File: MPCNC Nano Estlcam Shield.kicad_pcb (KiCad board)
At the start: 2 copper layers, 160 x 100 mm, 92 parts, among them J1 Screw_Terminal_01x02, J10 Conn_01x04_Male, J11 Conn_01x04_Male, J12 Screw_Terminal_01x03, J13 Screw_Terminal_01x03, J14 Screw_Terminal_01x03, J15 Conn_02x03_Odd_Even, J16 Screw_Terminal_01x02, J17 Screw_Terminal_01x02, J18 Screw_Terminal_01x03, J19 Screw_Terminal_01x03, J2 Conn_01x03_Male, J20 Screw_Terminal_01x03, J21 Screw_Terminal_01x03, J22 Screw_Terminal_01x03, J23 Screw_Terminal_01x03, J24 Screw_Terminal_01x03, J25 Screw_Terminal_01x03, J26 Screw_Terminal_01x03, J27 Screw_Terminal_01x03, J28 Conn_01x03_Male, J29 Conn_01x02_Male, J3 Conn_01x06_Male, J4 Screw_Terminal_01x03, J5 Screw_Terminal_01x03, J6 Screw_Terminal_01x03, J7 Conn_01x04_Male, J8 Conn_01x04_Male, J9 Conn_01x04_Male, U1 LM358, U2 LTV-847, U3 LTV-847, U4 LTV-847, U5 ULN2003, U6 L7805, U7 ATtiny45-20PU

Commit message: V1.3
- Version 1.3 of MPCNC Nano Estlcam Shield
   PCB schematic changes:
    # Changed electrolytic capacitor values for L7805 (0,33µF + 0,1µF)
   PCB layout changes:
    # Changed footprint of electrolytic capacitor for L7805 (D=8mm/RM=3,5mm -> D=5mm/RM=2,0mm)
    # Revised heatsink footprint
    + Footprints for many components added to project footprint library ("MPCNC_Shield_Footprints"). Modified footprints from standard KiCad library with value on
silkscreen
    + Added "Uncle Phil" logo on backside silk screen layer
    + Added jumper function description on frontside silk screen layer
    # Changed mounting holes (Edge.cut layer -> footprint)
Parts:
- added H1: MountingHole, MountingHole:MountingHole_4.3mm_M4_DIN965_Pad, F.Cu at (65.5, 137.3)
- added H2: MountingHole, MountingHole:MountingHole_4.3mm_M4_DIN965_Pad, F.Cu at (217.5, 137.3)
- added H3: MountingHole, MountingHole:MountingHole_4.3mm_M4_DIN965_Pad, F.Cu at (217.5, 45.4)
- added H4: MountingHole, MountingHole:MountingHole_4.3mm_M4_DIN965_Pad, F.Cu at (65.5, 45.4)
- A1: value Arduino_Nano_v3.x -> Arduino Nano
- C1, C2, C3, C4: footprint Capacitor_THT:CP_Radial_D8.0mm_P3.50mm -> MPCNC_Shield_Footprints:CP_Radial_D8.0mm_P3.50mm
- C5: value 1µF -> 0,33µF; footprint Capacitor_THT:CP_Radial_D8.0mm_P3.50mm -> Capacitor_THT:CP_Radial_D5.0mm_P2.00mm
- C6: value 1µF -> 0,1µF; footprint Capacitor_THT:CP_Radial_D8.0mm_P3.50mm -> Capacitor_THT:CP_Radial_D5.0mm_P2.00mm
- D2, D3: footprint Diode_THT:D_DO-201AD_P15.24mm_Horizontal -> MPCNC_Shield_Footprints:D_DO-201AD_P15.24mm_Horizontal
- R1, R10, R11, R12, R13, R14, R15, R16, R17, R18, R2, R3, R4, R5, R6, R7, R8, R9: footprint Resistor_THT:R_Axial_DIN0207_L6.3mm_D2.5mm_P7.62mm_Horizontal -> MPCNC_Shield_Footprints:R_Axial_DIN0207_L6.3mm_D2.5mm_P7.62mm_Horizontal
- U1: footprint Package_DIP:DIP-8_W7.62mm -> MPCNC_Shield_Footprints:DIP-8_W7.62mm
- U2, U3, U4, U5: footprint Package_DIP:DIP-16_W7.62mm -> MPCNC_Shield_Footprints:DIP-16_W7.62mm
- U7: footprint Package_DIP:DIP-8_W7.62mm_LongPads -> MPCNC_Shield_Footprints:DIP-8_W7.62mm
- moved R14 6.35 mm to (180.9, 103.9), turned to 0 degrees
- moved C5 3.70 mm to (163.1, 93.7)
- moved JP13 0.25 mm to (207.6, 129.9)
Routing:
- net /D1_R_LED: track 24.7 -> 15.8 mm
- net +5V: track 685.5 -> 679.4 mm
- net +12V: track 135.3 -> 132.0 mm
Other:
- outline, holes or cut-outs redrawn
- board text added: "12V"
- board text added: "5V"
- board text added: "5V/10V"
- board text added: "Adjust 0-10V"
- board text added: "Analog"
- board text added: "COM"
- board text added: "FLT"
- board text added: "Fan 12V"
- board text added: "ICSP"
- board text added: "MPCNC Nano Estlcam Shield © V1.3"
- board text added: "PWM"
- board text added: "Spindle On/Off"
- board text removed: "Adjust to 0-10V"
- board text removed: "FAN 12V"
- board text removed: "MPCNC Nano Estlcam Shield © V1.2"

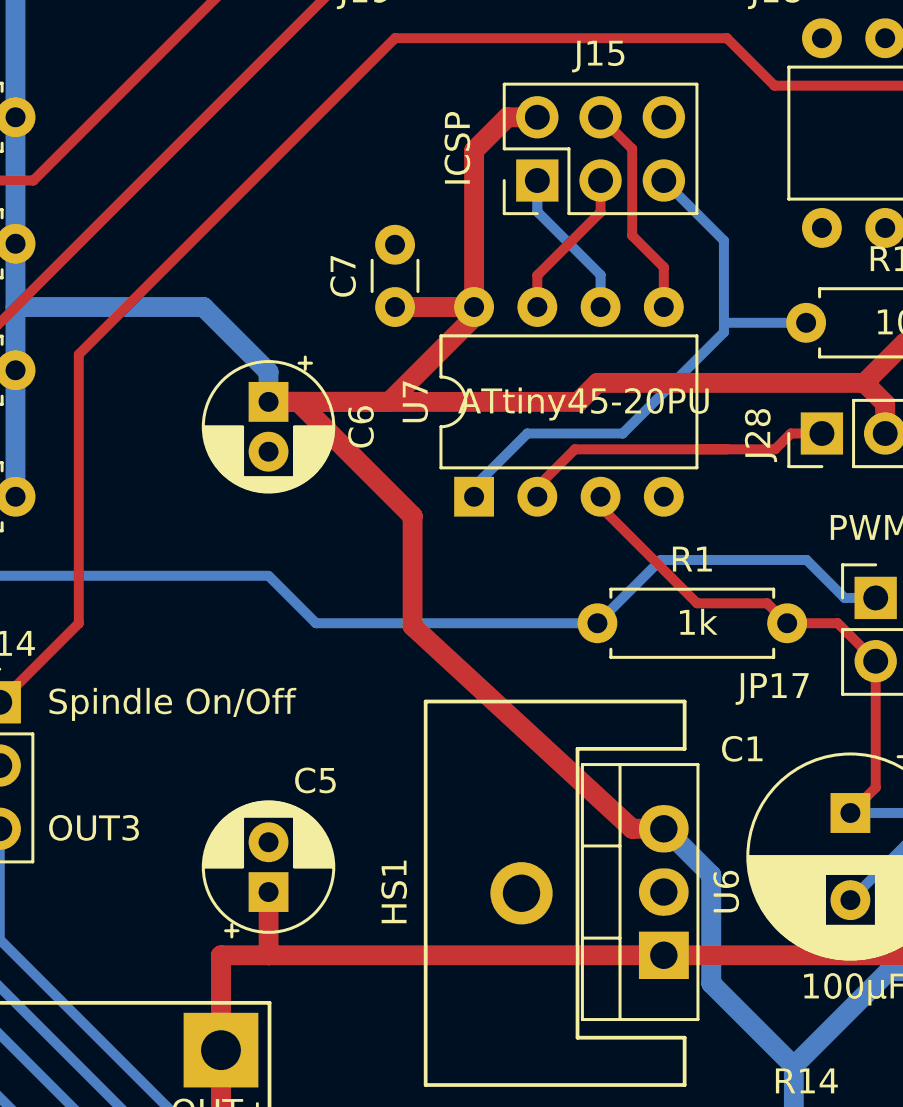
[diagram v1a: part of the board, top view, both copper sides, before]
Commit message: Minor changes for V1.3
   PCB schematic changes:
#Changed footprints for some parts from standard lib to MPCNC lib
   PCB layout changes:
#Added value to silk screen layer for some footprints
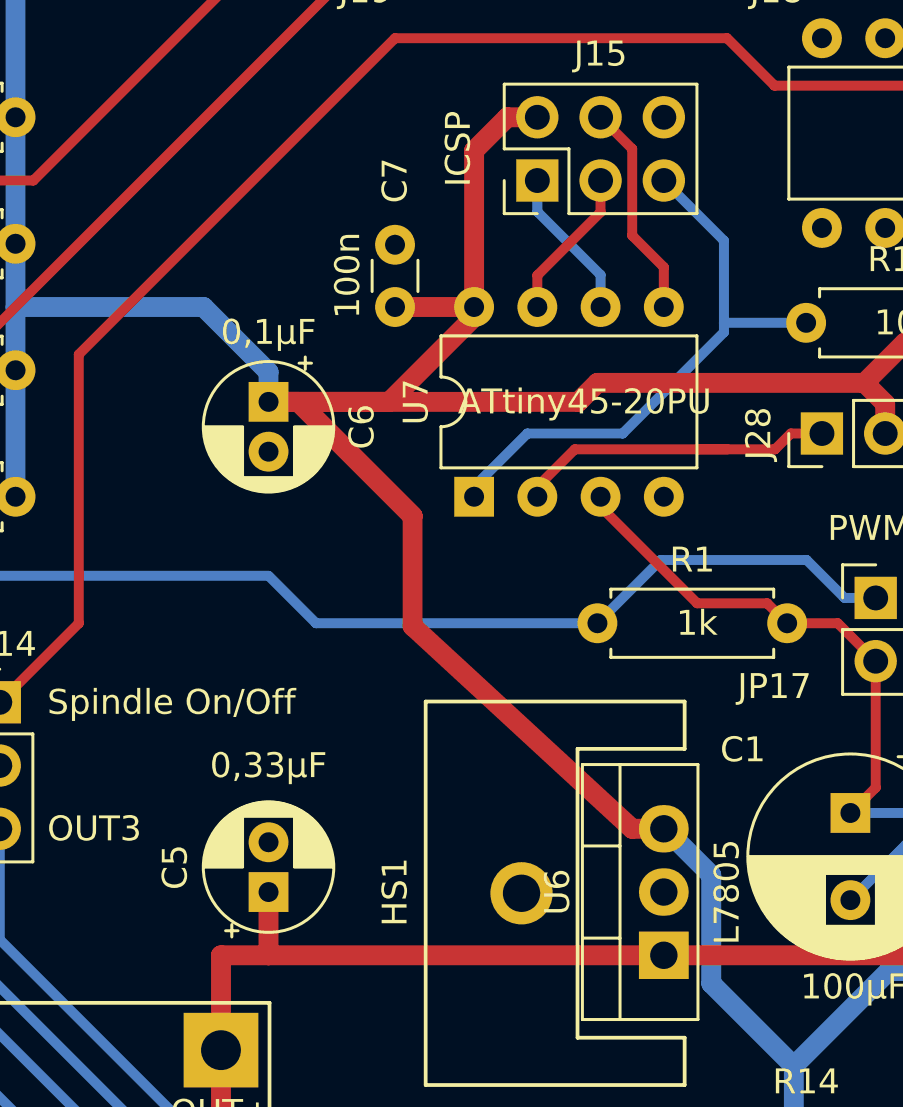
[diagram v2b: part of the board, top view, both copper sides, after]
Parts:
- C5, C6: footprint Capacitor_THT:CP_Radial_D5.0mm_P2.00mm -> MPCNC_Shield_Footprints:CP_Radial_D5.0mm_P2.00mm
- C7: footprint Capacitor_THT:C_Disc_D3.0mm_W1.6mm_P2.50mm -> MPCNC_Shield_Footprints:C_Disc_D3.0mm_W1.6mm_P2.50mm
- U6: footprint Package_TO_SOT_THT:TO-220-3_Vertical -> MPCNC_Shield_Footprints:TO-220-3_Vertical
